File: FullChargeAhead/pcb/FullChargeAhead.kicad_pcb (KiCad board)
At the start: 2 copper layers, 24.2 x 40.3 mm, 18 parts, among them CON101 USB-MICRO-B, P101 TIMER, P102 BATT, U101 MCP73834-FCI/UN

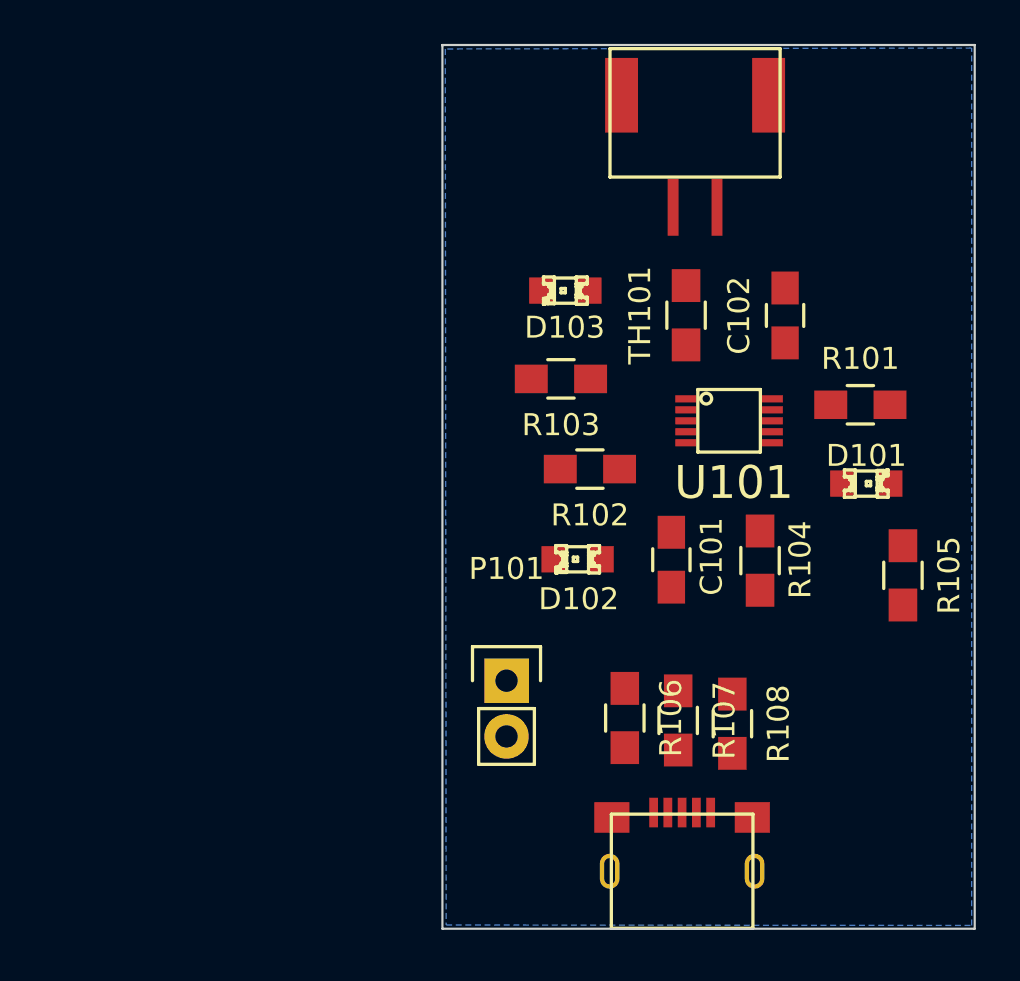
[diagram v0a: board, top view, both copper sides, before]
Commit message: First board layout complete and initial gerbers.
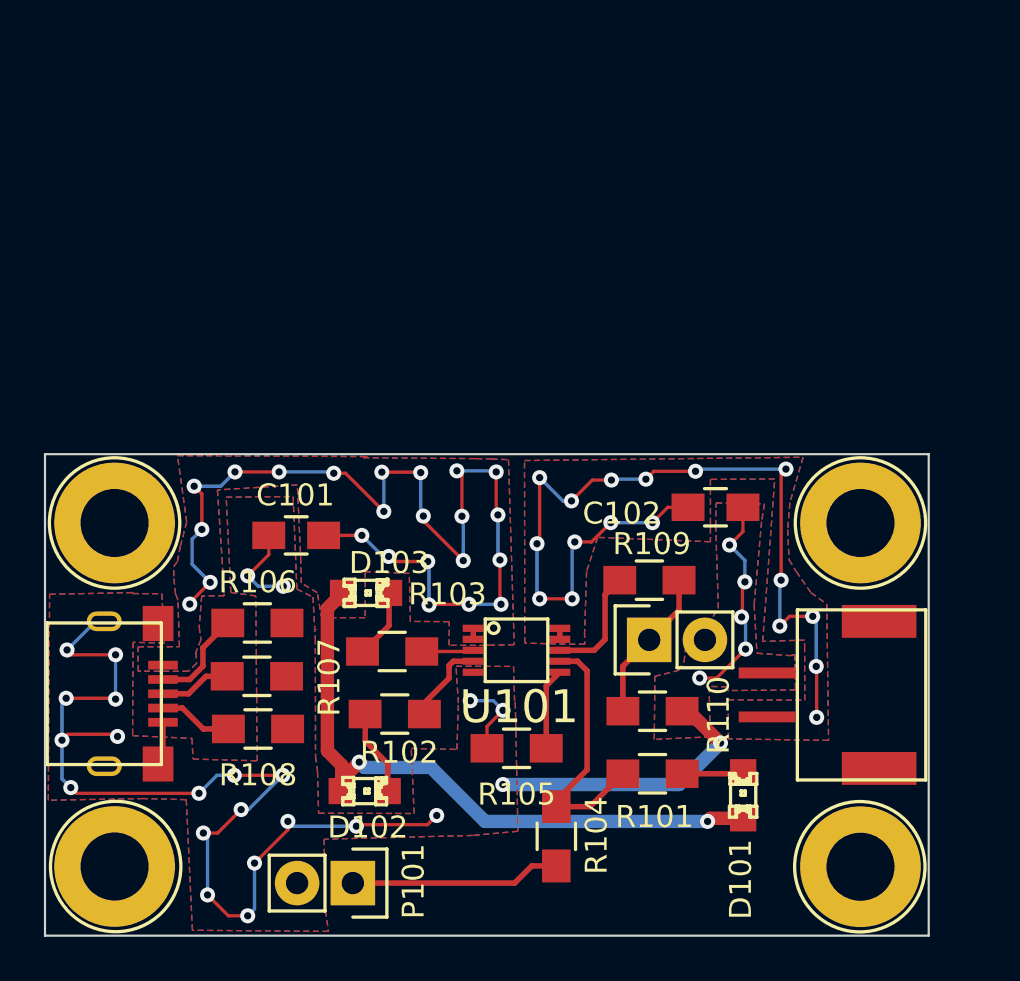
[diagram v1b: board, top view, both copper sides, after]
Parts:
- removed TH101: 10K, Resistors_SMD:R_0805_HandSoldering
- added P103: CONN_01X01, pcb:1pin_m3_screw, F.Cu at (81.4, 91.8)
- added P104: CONN_01X01, pcb:1pin_m3_screw, F.Cu at (81.3, 76.1)
- added P105: CONN_01X01, pcb:1pin_m3_screw, F.Cu at (115.3, 91.8)
- added P106: CONN_01X01, pcb:1pin_m3_screw, F.Cu at (115.3, 76.1)
- added P107: THERM, Pin_Headers:Pin_Header_Straight_1x02, F.Cu at (105.7, 81.5)
- added R109: 1.54K, Resistors_SMD:R_0805_HandSoldering, F.Cu at (105.7, 78.7)
- added R110: 69.8K, Resistors_SMD:R_0805_HandSoldering, F.Cu at (105.8, 84.7)
- moved P102 27.6 mm to (115.4, 84.0), turned to 90 degrees
- moved CON101 27.5 mm to (80.9, 83.9), turned to 270 degrees
- moved R108 21.6 mm to (87.9, 85.5), turned to 180 degrees
- moved R107 19.3 mm to (87.8, 83.1), turned to 180 degrees
- moved R101 19.3 mm to (105.8, 87.6)
- moved R105 19.3 mm to (99.7, 86.4), turned to 180 degrees
- moved R106 17.3 mm to (87.8, 80.7), turned to 180 degrees
- moved C101 17.1 mm to (89.6, 76.7), turned to 180 degrees
- moved D103 16.5 mm to (92.8, 79.3), turned to 0 degrees
- moved R104 15.6 mm to (101.5, 90.4)
- moved D101 15.3 mm to (110.0, 88.5), turned to 90 degrees
- moved R103 14.6 mm to (94.0, 82.0)
- moved D102 14.3 mm to (92.7, 88.3), turned to 0 degrees
- moved R102 14.3 mm to (94.1, 84.8)
- moved U101 14.3 mm to (99.6, 81.9)
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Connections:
- net Net-(C101-Pad1) renamed /Vdd
- net Net-(C102-Pad1) renamed /Vbat
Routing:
- net GND: track 0.00 -> 80.9 mm, vias 0 -> 29
- net /Vdd: track 0.00 -> 78.1 mm, vias 0 -> 25
- net /Vbat: track 0.00 -> 41.9 mm, vias 0 -> 17
- net Net-(R101-Pad1): track 0.00 -> 11.8 mm
- net Net-(P101-Pad1): track 0.00 -> 9.59 mm
- net Net-(P107-Pad1): track 0.00 -> 7.03 mm
- net Net-(R109-Pad1): track 0.00 -> 5.24 mm
- net Net-(CON101-Pad2): track 0.00 -> 4.51 mm
- net Net-(R102-Pad1): track 0.00 -> 4.24 mm
- net Net-(D102-Pad2): track 0.00 -> 3.94 mm
- net Net-(R105-Pad1): track 0.00 -> 3.72 mm
- net Net-(CON101-Pad4): track 0.00 -> 3.38 mm
- net Net-(CON101-Pad3): track 0.00 -> 3.26 mm
- net Net-(D103-Pad2): track 0.00 -> 3.19 mm
- net Net-(D101-Pad2): track 0.00 -> 2.81 mm
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- added copper zone on B.Cu, net /Vbat
- added copper zone on F.Cu, net /Vbat
- added copper zone on B.Cu, net /Vdd
- added copper zone on F.Cu, net /Vdd
- added copper zone on F.Cu, net GND
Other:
- board size 24.2 x 40.3 mm -> 40.3 x 21.9 mm
- net class Default: clearance 0.254 -> 0.152; trace_width 0.254 -> 0.152; via_dia 0.889 -> 0.686; via_drill 0.635 -> 0.33
- net class Default1 added: clearance 0.254, trace_width 0.254, via_dia 0.889, via_drill 0.635
- net class PWR added: clearance 0.305, trace_width 0.61, via_dia 1.143, via_drill 0.762
- rule trace_clearance: 0.254 -> 0.152
- rule trace_min: 0.254 -> 0.152
- rule via_min_drill: 0.508 -> 0.33
- rule via_min_size: 0.889 -> 0.686
- board text added: "Brooke Hedrick"
- board text added: "Creative Commons: CC-BY 03.23.2015"
- board text added: "FullChargeAhead : fca_v1"
- board text added: "brooke.t.hedrick@gmail.com"
- board text added: "https://github.com/hedrickbt/ContextualElectronics.git"
